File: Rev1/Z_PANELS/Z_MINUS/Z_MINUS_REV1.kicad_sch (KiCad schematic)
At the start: 0 parts

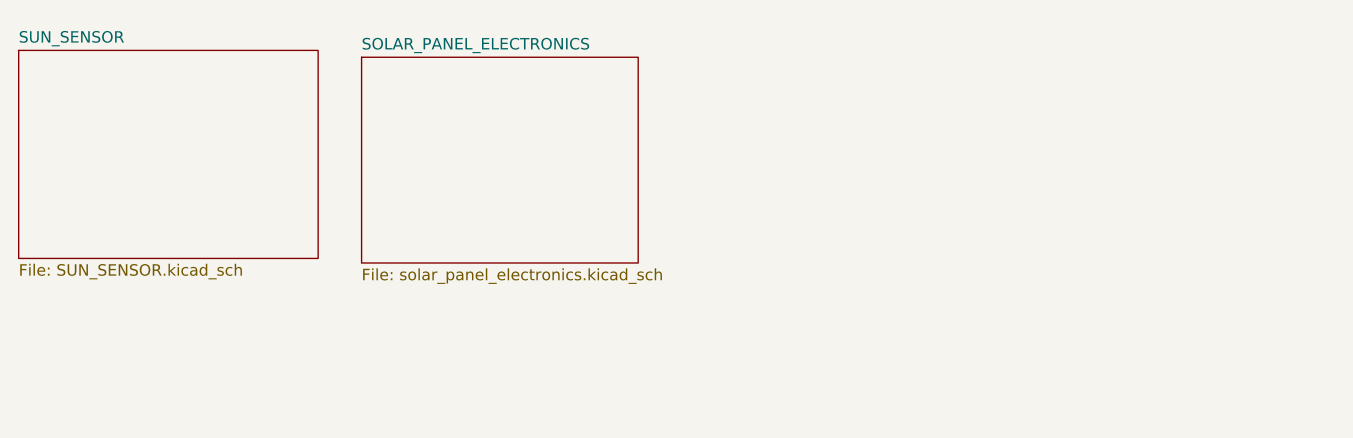
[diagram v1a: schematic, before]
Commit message: finished Z minus board design
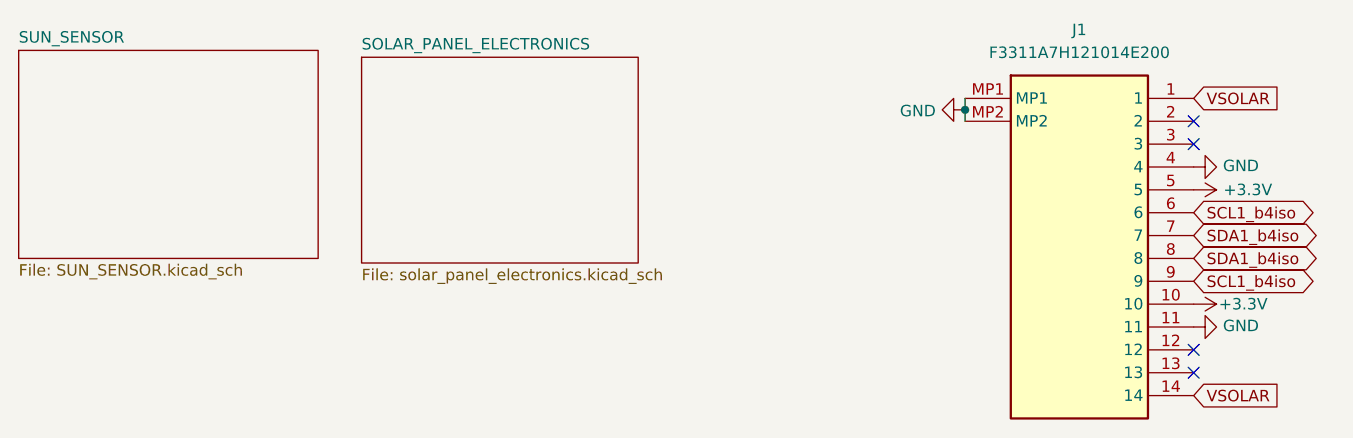
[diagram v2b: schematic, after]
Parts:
- added J1: F3311A7H121014E200, F3311A7H121014E200, symbol F3311A7H121008E200:F3311A7H121014E200
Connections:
- new net +3.3V: J1.10, J1.5
- new net GND: J1.11, J1.4, J1.MP1, J1.MP2
- new net SCL1_b4iso: J1.6, J1.9
- new net SDA1_b4iso: J1.7, J1.8
- new net VSOLAR: J1.1, J1.14
- no-connect marks 0 -> 4
